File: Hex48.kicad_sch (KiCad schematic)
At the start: 18 parts, among them J1 Conn_02x24_Counter_Clockwise, J2 Conn_02x24_Odd_Even, J3 Conn_02x24_Odd_Even, J4 Conn_02x02_Odd_Even, J5 Conn_02x02_Odd_Even, J6 Conn_02x24_Odd_Even, J7 Conn_02x12_Counter_Clockwise, J8 Conn_02x12_Counter_Clockwise, SW1 SW_Push, SW2 SW_Push

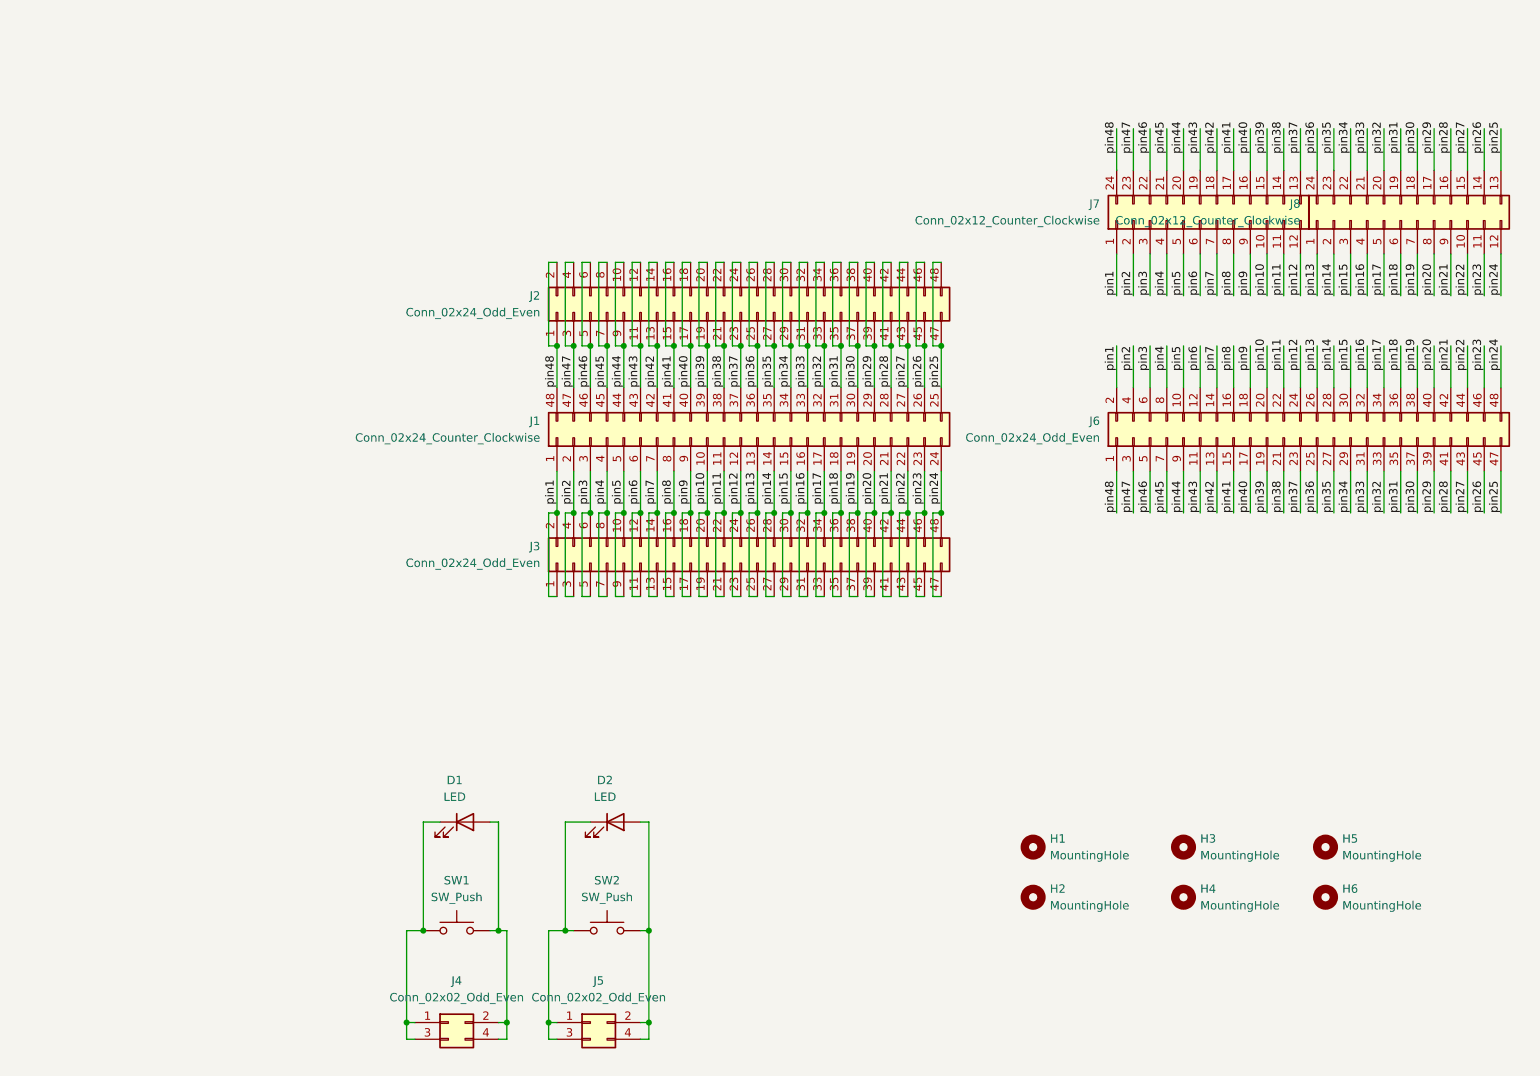
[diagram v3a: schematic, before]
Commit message: Finish schematic, map all footprints,update PCB.
Rats-nest now complete. Some parts placed on PCB in final locations. Some parts (mounting holes and 2x8 headers) need to be placed exactly on a polar grid at 60-degree intervals.
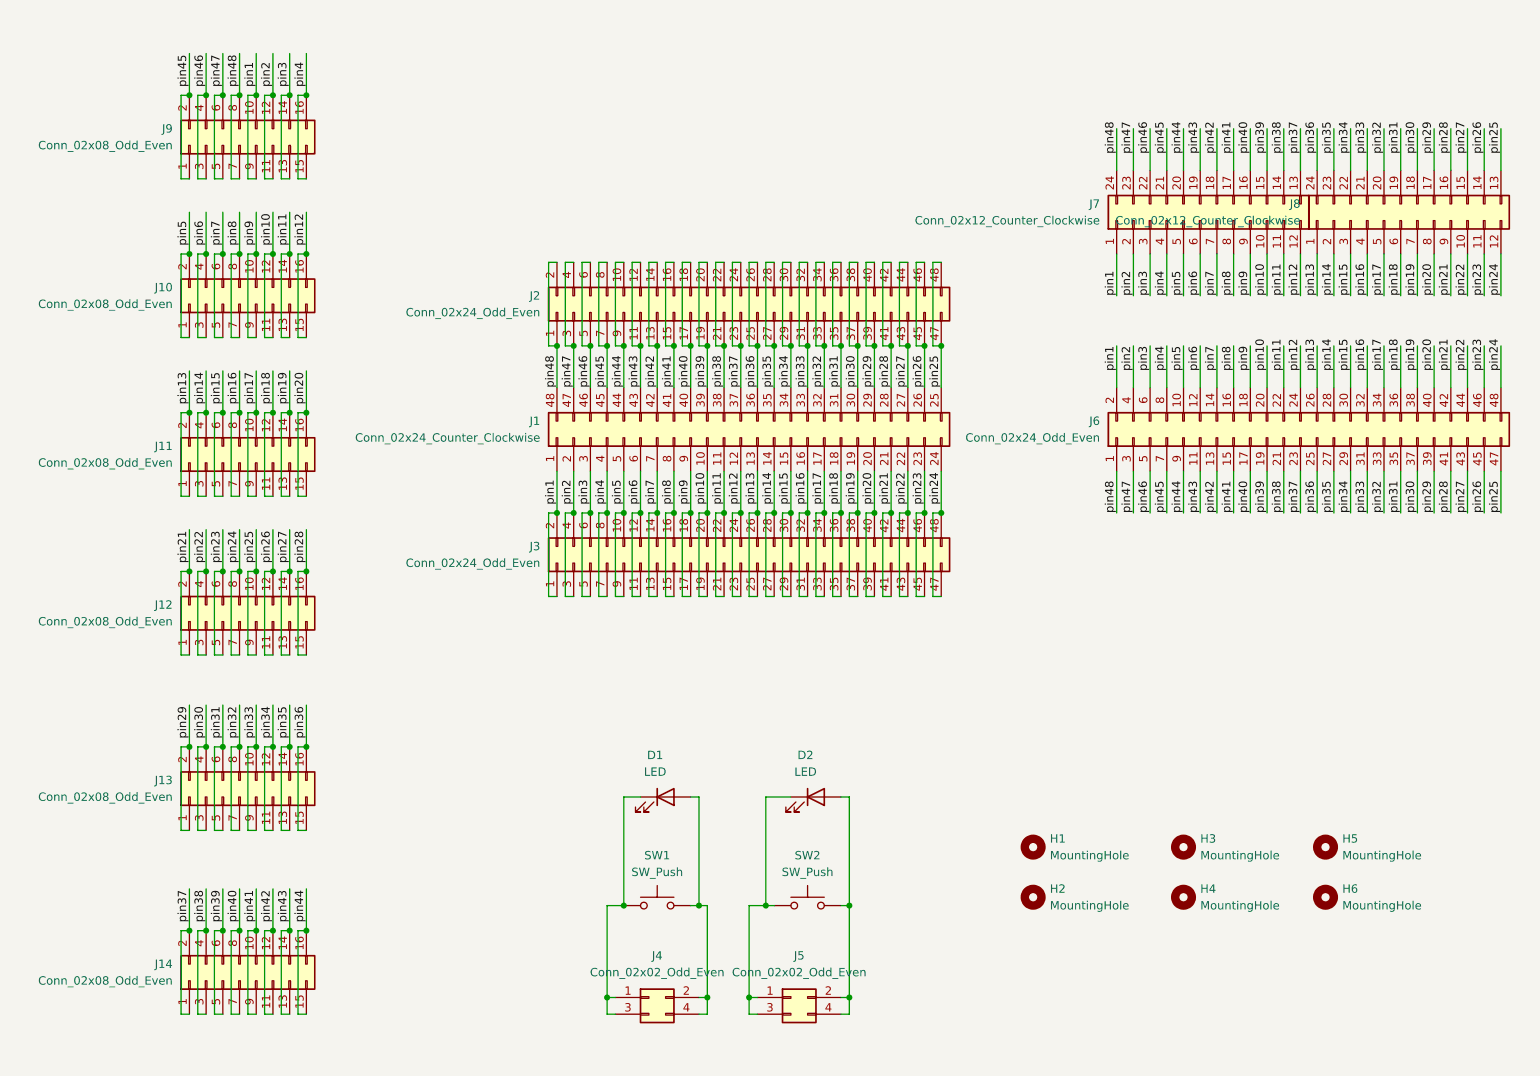
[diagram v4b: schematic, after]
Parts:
- added J10, J11, J12, J13, J14, J9: Conn_02x08_Odd_Even, Connector_PinSocket_2.54mm:PinSocket_2x08_P2.54mm_Vertical, symbol Connector_Generic:Conn_02x08_Odd_Even
- H1, H2, H3, H4, H5, H6: footprint MountingHole:MountingHole_3.2mm_M3_Pad_TopBottom -> MountingHole:MountingHole_3.2mm_M3_Pad
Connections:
- net pin1: now also J9.10 (Pin_10), J9.9 (Pin_9)
- net pin10: now also J10.11 (Pin_11), J10.12 (Pin_12)
- net pin11: now also J10.13 (Pin_13), J10.14 (Pin_14)
- net pin12: now also J10.15 (Pin_15), J10.16 (Pin_16)
- net pin13: now also J11.1 (Pin_1), J11.2 (Pin_2)
- net pin14: now also J11.3 (Pin_3), J11.4 (Pin_4)
- net pin15: now also J11.5 (Pin_5), J11.6 (Pin_6)
- net pin16: now also J11.7 (Pin_7), J11.8 (Pin_8)
- net pin17: now also J11.10 (Pin_10), J11.9 (Pin_9)
- net pin18: now also J11.11 (Pin_11), J11.12 (Pin_12)
- net pin19: now also J11.13 (Pin_13), J11.14 (Pin_14)
- net pin2: now also J9.11 (Pin_11), J9.12 (Pin_12)
- net pin20: now also J11.15 (Pin_15), J11.16 (Pin_16)
- net pin21: now also J12.1 (Pin_1), J12.2 (Pin_2)
- net pin22: now also J12.3 (Pin_3), J12.4 (Pin_4)
- net pin23: now also J12.5 (Pin_5), J12.6 (Pin_6)
- net pin24: now also J12.7 (Pin_7), J12.8 (Pin_8)
- net pin25: now also J12.10 (Pin_10), J12.9 (Pin_9)
- net pin26: now also J12.11 (Pin_11), J12.12 (Pin_12)
- net pin27: now also J12.13 (Pin_13), J12.14 (Pin_14)
- net pin28: now also J12.15 (Pin_15), J12.16 (Pin_16)
- net pin29: now also J13.1 (Pin_1), J13.2 (Pin_2)
- net pin3: now also J9.13 (Pin_13), J9.14 (Pin_14)
- net pin30: now also J13.3 (Pin_3), J13.4 (Pin_4)
- net pin31: now also J13.5 (Pin_5), J13.6 (Pin_6)
- net pin32: now also J13.7 (Pin_7), J13.8 (Pin_8)
- net pin33: now also J13.10 (Pin_10), J13.9 (Pin_9)
- net pin34: now also J13.11 (Pin_11), J13.12 (Pin_12)
- net pin35: now also J13.13 (Pin_13), J13.14 (Pin_14)
- net pin36: now also J13.15 (Pin_15), J13.16 (Pin_16)
- net pin37: now also J14.1 (Pin_1), J14.2 (Pin_2)
- net pin38: now also J14.3 (Pin_3), J14.4 (Pin_4)
- net pin39: now also J14.5 (Pin_5), J14.6 (Pin_6)
- net pin4: now also J9.15 (Pin_15), J9.16 (Pin_16)
- net pin40: now also J14.7 (Pin_7), J14.8 (Pin_8)
- net pin41: now also J14.10 (Pin_10), J14.9 (Pin_9)
- net pin42: now also J14.11 (Pin_11), J14.12 (Pin_12)
- net pin43: now also J14.13 (Pin_13), J14.14 (Pin_14)
- net pin44: now also J14.15 (Pin_15), J14.16 (Pin_16)
- net pin45: now also J9.1 (Pin_1), J9.2 (Pin_2)
- net pin46: now also J9.3 (Pin_3), J9.4 (Pin_4)
- net pin47: now also J9.5 (Pin_5), J9.6 (Pin_6)
- net pin48: now also J9.7 (Pin_7), J9.8 (Pin_8)
- net pin5: now also J10.1 (Pin_1), J10.2 (Pin_2)
- net pin6: now also J10.3 (Pin_3), J10.4 (Pin_4)
- net pin7: now also J10.5 (Pin_5), J10.6 (Pin_6)
- net pin8: now also J10.7 (Pin_7), J10.8 (Pin_8)
- net pin9: now also J10.10 (Pin_10), J10.9 (Pin_9)
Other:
- moved on the sheet: D1, D2, J4, J5, SW1, SW2

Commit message: Final schematic, V1.0.
Add some text comments.
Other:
- note added: "2x24 pin female header"
- note added: "2x24 pin female header in centre"
- note added: "48-pin 0.6in DIL socket"
- note added: "Optional LEDs and switches"
- note added: "Six 2x8 pin female headers as sides of hexagon"
- note added: "Two 24-pin 0.3in DIL sockets"
- moved on the sheet: J8
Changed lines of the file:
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@@
 	(title_block
 		(title "Hex48 Prototyping Board")
-		(date "2024-10-09")
-		(rev "0.2")
+		(date "2024-10-11")
+		(rev "1.0")
 		(company "John Honniball")
 		(comment 1 "Hexagonal DIL breadboard")
@@
 	(wire
 		(pts
-			(xy 247.65 43.18) (xy 247.65 49.53)
+			(xy 250.19 43.18) (xy 250.19 49.53)
 		)
 		(stroke
@@
 	(wire
 		(pts
-			(xy 219.71 43.18) (xy 219.71 49.53)
+			(xy 222.25 43.18) (xy 222.25 49.53)
 		)
 		(stroke
@@
 	(wire
 		(pts
-			(xy 237.49 62.23) (xy 237.49 68.58)
+			(xy 240.03 62.23) (xy 240.03 68.58)
 		)
 		(stroke
@@
 	(wire
 		(pts
-			(xy 234.95 43.18) (xy 234.95 49.53)
+			(xy 237.49 43.18) (xy 237.49 49.53)
 		)
 		(stroke
@@
 	(wire
 		(pts
-			(xy 237.49 43.18) (xy 237.49 49.53)
+			(xy 240.03 43.18) (xy 240.03 49.53)
 		)
 		(stroke
@@
 	(wire
 		(pts
-			(xy 245.11 62.23) (xy 245.11 68.58)
+			(xy 247.65 62.23) (xy 247.65 68.58)
 		)
 		(stroke
@@
 	(wire
 		(pts
-			(xy 242.57 43.18) (xy 242.57 49.53)
+			(xy 245.11 43.18) (xy 245.11 49.53)
 		)
 		(stroke
@@
 	(wire
 		(pts
-			(xy 245.11 43.18) (xy 245.11 49.53)
+			(xy 247.65 43.18) (xy 247.65 49.53)
 		)
 		(stroke
@@
 	(wire
 		(pts
-			(xy 232.41 43.18) (xy 232.41 49.53)
+			(xy 234.95 43.18) (xy 234.95 49.53)
 		)
 		(stroke
@@
 	(wire
 		(pts
-			(xy 240.03 62.23) (xy 240.03 68.58)
+			(xy 242.57 62.23) (xy 242.57 68.58)
 		)
 		(stroke
@@
 	(wire
 		(pts
-			(xy 247.65 62.23) (xy 247.65 68.58)
+			(xy 250.19 62.23) (xy 250.19 68.58)
 		)
 		(stroke
@@
 	(wire
 		(pts
-			(xy 229.87 62.23) (xy 229.87 68.58)
+			(xy 232.41 62.23) (xy 232.41 68.58)
 		)
 		(stroke
@@
 	(wire
 		(pts
-			(xy 224.79 43.18) (xy 224.79 49.53)
+			(xy 227.33 43.18) (xy 227.33 49.53)
 		)
 		(stroke
@@
 	(wire
 		(pts
-			(xy 229.87 43.18) (xy 229.87 49.53)
+			(xy 232.41 43.18) (xy 232.41 49.53)
 		)
 		(stroke
@@
 	(wire
 		(pts
-			(xy 227.33 43.18) (xy 227.33 49.53)
+			(xy 229.87 43.18) (xy 229.87 49.53)
 		)
 		(stroke
@@
 	(wire
 		(pts
-			(xy 240.03 43.18) (xy 240.03 49.53)
+			(xy 242.57 43.18) (xy 242.57 49.53)
 		)
 		(stroke
@@
 	(wire
 		(pts
-			(xy 222.25 62.23) (xy 222.25 68.58)
+			(xy 224.79 62.23) (xy 224.79 68.58)
 		)
 		(stroke
@@
 	(wire
 		(pts
-			(xy 232.41 62.23) (xy 232.41 68.58)
+			(xy 234.95 62.23) (xy 234.95 68.58)
 		)
 		(stroke
@@
 	(wire
 		(pts
-			(xy 242.57 62.23) (xy 242.57 68.58)
+			(xy 245.11 62.23) (xy 245.11 68.58)
 		)
 		(stroke
@@
 	(wire
 		(pts
-			(xy 224.79 62.23) (xy 224.79 68.58)
+			(xy 227.33 62.23) (xy 227.33 68.58)
 		)
 		(stroke
@@
 	(wire
 		(pts
-			(xy 222.25 43.18) (xy 222.25 49.53)
+			(xy 224.79 43.18) (xy 224.79 49.53)
 		)
 		(stroke
@@
 	(wire
 		(pts
-			(xy 234.95 62.23) (xy 234.95 68.58)
+			(xy 237.49 62.23) (xy 237.49 68.58)
 		)
 		(stroke
@@
 	(wire
 		(pts
-			(xy 227.33 62.23) (xy 227.33 68.58)
+			(xy 229.87 62.23) (xy 229.87 68.58)
 		)
 		(stroke
@@
 	(wire
 		(pts
-			(xy 219.71 62.23) (xy 219.71 68.58)
+			(xy 222.25 62.23) (xy 222.25 68.58)
 		)
 		(stroke
@@
 		)
 	)
+	(text "2x24 pin female header"
+		(exclude_from_sim no)
+		(at 134.62 118.364 0)
+		(effects
+			(font
+				(size 1.27 1.27)
+			)
+		)
+	)
+	(text "Six 2x8 pin female headers as sides of hexagon"
+		(exclude_from_sim no)
+		(at 56.642 27.178 0)
+		(effects
+			(font
+				(size 1.27 1.27)
+			)
+		)
+	)
+	(text "Optional LEDs and switches"
+		(exclude_from_sim no)
+		(at 129.794 184.15 0)
+		(effects
+			(font
+				(size 1.27 1.27)
+			)
+		)
+	)
+	(text "Two 24-pin 0.3in DIL sockets"
+		(exclude_from_sim no)
+		(at 218.694 37.846 0)
+		(effects
+			(font
+				(size 1.27 1.27)
+			)
+		)
+	)
+	(text "2x24 pin female header in centre"
+		(exclude_from_sim no)
+		(at 219.71 104.902 0)
+		(effects
+			(font
+				(size 1.27 1.27)
+			)
+		)
+	)
+	(text "48-pin 0.6in DIL socket"
+		(exclude_from_sim no)
+		(at 86.36 87.884 0)
+		(effects
+			(font
+				(size 1.27 1.27)
+			)
+		)
+	)
+	(text "2x24 pin female header"
+		(exclude_from_sim no)
+		(at 132.334 60.706 0)
+		(effects
+			(font
+				(size 1.27 1.27)
+			)
+		)
+	)
 	(label "pin40"
 		(at 209.55 101.6 90)
@@
 	)
 	(label "pin36"
-		(at 219.71 46.99 90)
+		(at 222.25 46.99 90)
 		(fields_autoplaced yes)
 		(effects
@@
 	)
 	(label "pin20"
-		(at 237.49 68.58 90)
+		(at 240.03 68.58 90)
 		(fields_autoplaced yes)
 		(effects
@@
 	)
 	(label "pin24"
-		(at 247.65 68.58 90)
+		(at 250.19 68.58 90)
 		(fields_autoplaced yes)
 		(effects
@@
 	)
 	(label "pin32"
-		(at 229.87 46.99 90)
+		(at 232.41 46.99 90)
 		(fields_autoplaced yes)
 		(effects
@@
 	)
 	(label "pin28"
-		(at 240.03 46.99 90)
+		(at 242.57 46.99 90)
 		(fields_autoplaced yes)
 		(effects
@@
 	)
 	(label "pin26"
-		(at 245.11 46.99 90)
+		(at 247.65 46.99 90)
 		(fields_autoplaced yes)
 		(effects
@@
 	)
 	(label "pin17"
-		(at 229.87 68.58 90)
+		(at 232.41 68.58 90)
 		(fields_autoplaced yes)
 		(effects
@@
 	)
 	(label "pin14"
-		(at 222.25 68.58 90)
+		(at 224.79 68.58 90)
 		(fields_autoplaced yes)
 		(effects
@@
 	)
 	(label "pin18"
-		(at 232.41 68.58 90)
+		(at 234.95 68.58 90)
 		(fields_autoplaced yes)
 		(effects
@@
 	)
 	(label "pin35"
-		(at 222.25 46.99 90)
+		(at 224.79 46.99 90)
 		(fields_autoplaced yes)
 		(effects
@@
 	)
 	(label "pin27"
-		(at 242.57 46.99 90)
+		(at 245.11 46.99 90)
 		(fields_autoplaced yes)
 		(effects
@@
 	)
 	(label "pin23"
-		(at 245.11 68.58 90)
+		(at 247.65 68.58 90)
 		(fields_autoplaced yes)
 		(effects
@@
 	)
 	(label "pin30"
-		(at 234.95 46.99 90)
+		(at 237.49 46.99 90)
 		(fields_autoplaced yes)
 		(effects
@@
 	)
 	(label "pin19"
-		(at 234.95 68.58 90)
+		(at 237.49 68.58 90)
 		(fields_autoplaced yes)
 		(effects
@@
 	)
 	(label "pin29"
-		(at 237.49 46.99 90)
+		(at 240.03 46.99 90)
 		(fields_autoplaced yes)
 		(effects
@@
 	)
 	(label "pin22"
-		(at 242.57 68.58 90)
+		(at 245.11 68.58 90)
 		(fields_autoplaced yes)
 		(effects
@@
 	)
 	(label "pin33"
-		(at 227.33 46.99 90)
+		(at 229.87 46.99 90)
 		(fields_autoplaced yes)
 		(effects
@@
 	)
 	(label "pin16"
-		(at 227.33 68.58 90)
+		(at 229.87 68.58 90)
 		(fields_autoplaced yes)
 		(effects
@@
 	)
 	(label "pin25"
-		(at 247.65 46.99 90)
+		(at 250.19 46.99 90)
 		(fields_autoplaced yes)
 		(effects
@@
 	)
 	(label "pin31"
-		(at 232.41 46.99 90)
+		(at 234.95 46.99 90)
 		(fields_autoplaced yes)
 		(effects
@@
 	)
 	(label "pin21"
-		(at 240.03 68.58 90)
+		(at 242.57 68.58 90)
 		(fields_autoplaced yes)
 		(effects
@@
 	)
 	(label "pin34"
-		(at 224.79 46.99 90)
+		(at 227.33 46.99 90)
 		(fields_autoplaced yes)
 		(effects
@@
 	)
 	(label "pin13"
-		(at 219.71 68.58 90)
+		(at 222.25 68.58 90)
 		(fields_autoplaced yes)
 		(effects
@@
 	)
 	(label "pin15"
-		(at 224.79 68.58 90)
+		(at 227.33 68.58 90)
 		(fields_autoplaced yes)
 		(effects
@@
 	(symbol
 		(lib_id "Connector_Generic:Conn_02x12_Counter_Clockwise")
-		(at 232.41 57.15 90)
+		(at 234.95 57.15 90)
 		(unit 1)
 		(exclude_from_sim no)
@@
 		(fields_autoplaced yes)
 		(property "Reference" "J8"
-			(at 217.17 54.6099 90)
+			(at 219.71 54.6099 90)
 			(effects
 				(font
@@
 		)
 		(property "Value" "Conn_02x12_Counter_Clockwise"
-			(at 217.17 57.1499 90)
+			(at 219.71 57.1499 90)
 			(effects
 				(font
@@
 		)
 		(property "Footprint" "Package_DIP:DIP-24_W7.62mm_Socket_LongPads"
-			(at 232.41 57.15 0)
+			(at 234.95 57.15 0)
 			(effects
 				(font
@@
 		)
 		(property "Datasheet" "~"
-			(at 232.41 57.15 0)
+			(at 234.95 57.15 0)
 			(effects
 				(font
@@
 		)
 		(property "Description" "Generic connector, double row, 02x12, counter clockwise pin numbering scheme (similar to DIP package numbering), script generated (kicad-library-utils/schlib/autogen/connector/)"
-			(at 232.41 57.15 0)
+			(at 234.95 57.15 0)
 			(effects
 				(font
